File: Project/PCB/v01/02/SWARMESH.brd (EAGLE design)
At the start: 75 x 75 mm, 51 parts, among them T5 TIP122TIP122, U1 ESP32DEVKITC, U2 TCRT5000L, U3 L293D, U4 L7805CV, U5 TCRT5000L, U6 CD4051BEE4

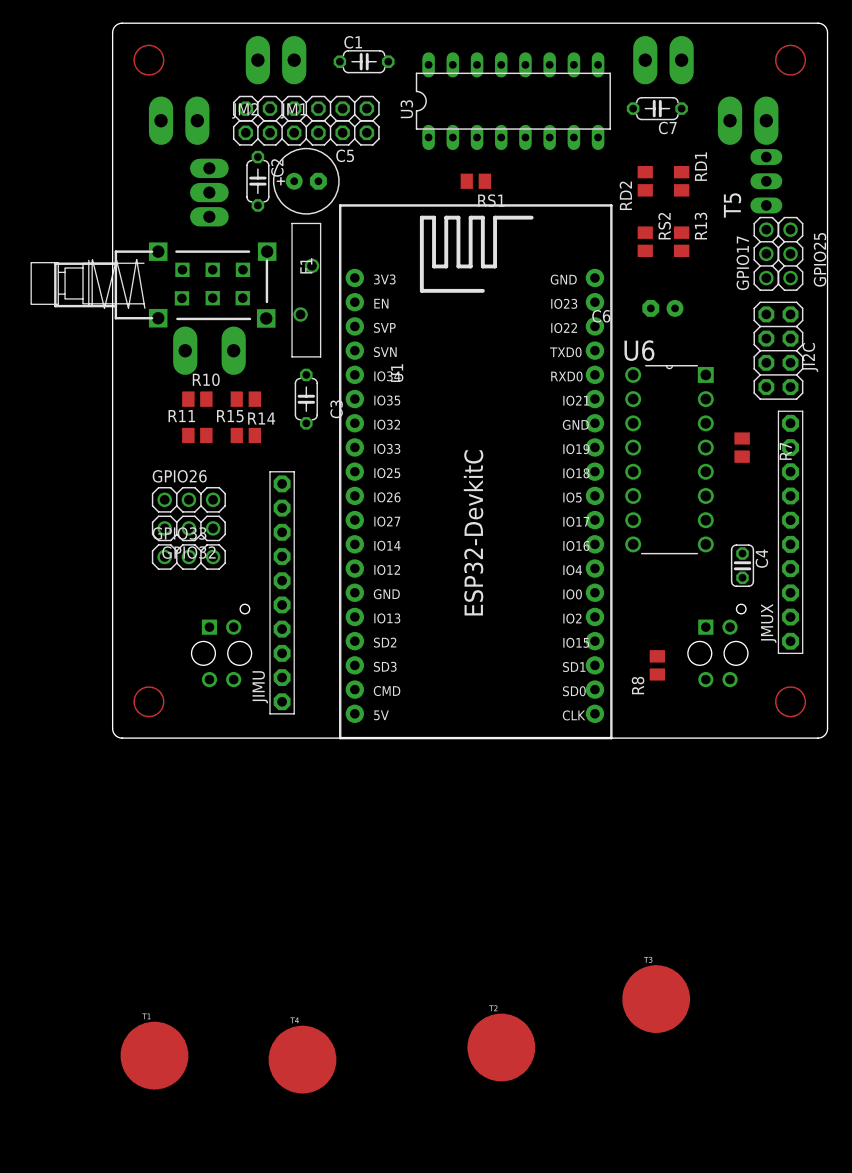
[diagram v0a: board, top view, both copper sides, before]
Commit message: add led PCB
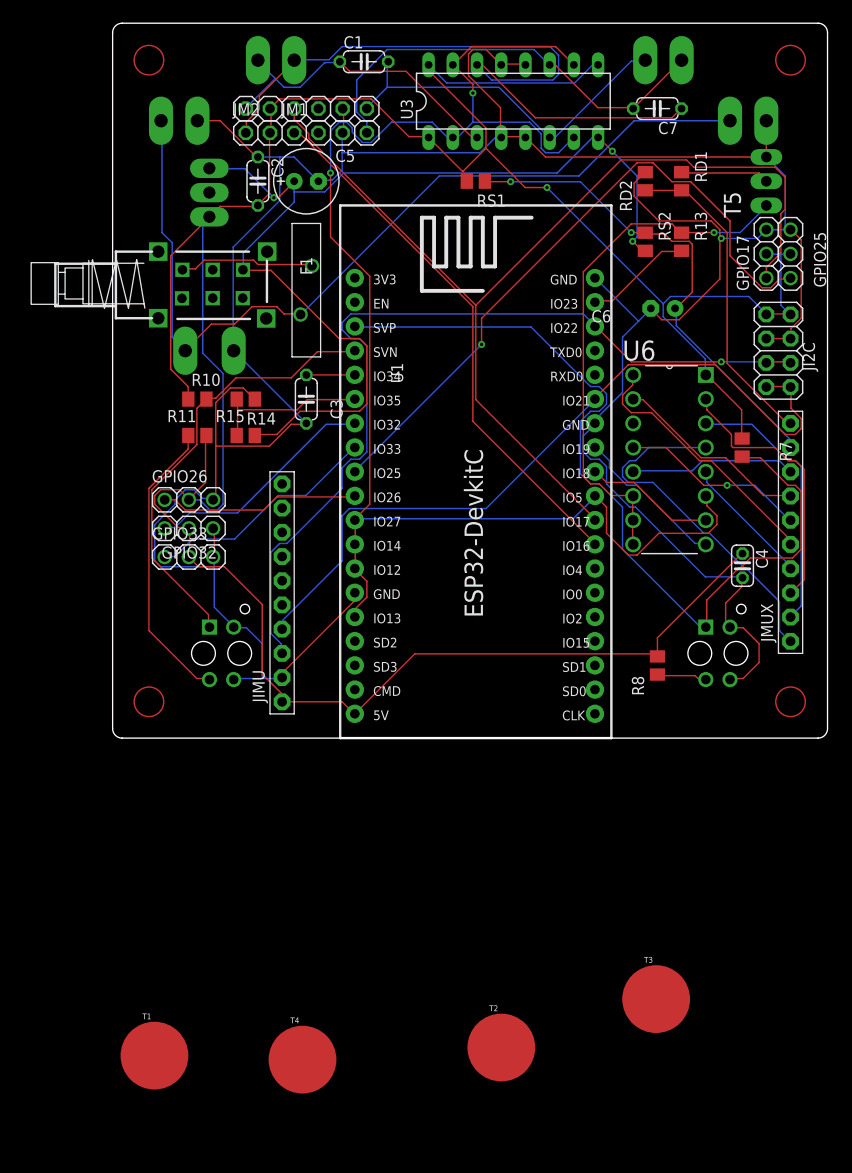
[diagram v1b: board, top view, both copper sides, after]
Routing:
- net GND: track 0.00 -> 328.8 mm, vias 0 -> 1
- net VCC: track 0.00 -> 298.0 mm, vias 0 -> 1
- net IO5: track 0.00 -> 155.9 mm, vias 0 -> 2
- net E1A: track 0.00 -> 107.2 mm
- net V+: track 0.00 -> 106.8 mm, vias 0 -> 3
- net N$15: track 0.00 -> 93.1 mm
- net SCL: track 0.00 -> 91.7 mm, vias 0 -> 1
- net IR1: track 0.00 -> 90.6 mm
- net SDA: track 0.00 -> 80.0 mm
- net M2A: track 0.00 -> 74.1 mm
- net IO25: track 0.00 -> 68.8 mm, vias 0 -> 1
- net E2A: track 0.00 -> 56.6 mm
- net N$12: track 0.00 -> 55.6 mm, vias 0 -> 1
- net N$16: track 0.00 -> 51.7 mm, vias 0 -> 2
- net IR2: track 0.00 -> 46.5 mm
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
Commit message: component placement
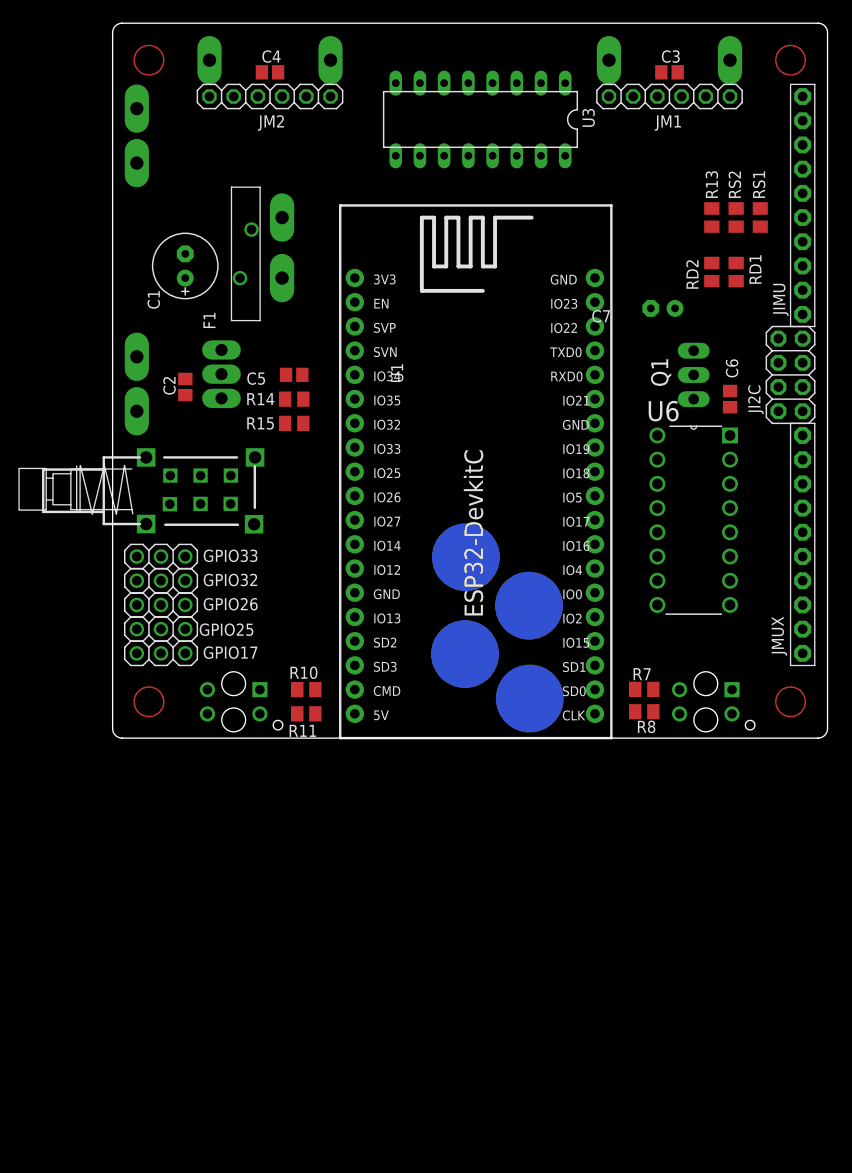
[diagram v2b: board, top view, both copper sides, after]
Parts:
- removed S2: (no value), ArduinoNano LearningBot 4-21-18:PS22F03
- removed T5: TIP122TIP122, TIP122(2):TIP122MODIFIED
- added Q1: TIP122TIP122, TIP122(2):TIP122MODIFIED
- added S1: (no value), ArduinoNano LearningBot 4-21-18:PS22F03
- C1, C7: value 0.1uF -> 10uF; device adafruit:C050-024X044 -> adafruit:E2,5-7
- C2, C3: value 0.1uF -> (none); device adafruit:C050-024X044 -> adafruit:C0805
- C4: value 0.1uF -> (none); device rcl:C025-024X044 -> adafruit:C0805
- C5, C6: value 10uF -> (none); device adafruit:E2,5-7 -> adafruit:C0805
- F1: value 30R400UF -> (none)
- moved GPIO25 76.9 mm to (5.08, 11.4), turned to 180 degrees
- moved GPIO17 76.1 mm to (5.08, 8.89), turned to 180 degrees
- moved C4 71.7 mm to (16.5, 69.8), turned to 0 degrees
- moved JIMU 68.1 mm to (72.4, 55.9)
- moved T4 55.4 mm to (37.1, 19.0), flipped to the bottom
- moved T1 54.3 mm to (43.8, 4.16), flipped to the bottom
- moved BAT- 53.4 mm to (17.8, 48.3)
- moved C3 51.3 mm to (58.4, 69.8), turned to 0 degrees
- moved CHG2+ 48.1 mm to (17.8, 54.6)
- moved T3 43.4 mm to (43.7, 13.9), flipped to the bottom
- moved T2 41.5 mm to (37.0, 8.81), flipped to the bottom
- moved JM1 38.1 mm to (58.4, 67.3)
- moved JP1 36.8 mm to (52.1, 71.1)
- moved JP3 36.8 mm to (22.9, 71.1)
- moved R10 32.6 mm to (20.3, 5.08), turned to 180 degrees
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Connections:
- removed net ADCMX1: U6.3
- new net IO12: U1.13, U3.15
- new net IO13: U1.15, U3.10
- new net IO14: U1.12, U3.2
- new net IO27: U1.11, U3.7
- net ADCMX: now also C5.1, U6.3; no longer C3.1
- net GND: now also C1.-, C5.2, C6.2, C7.-, Q1.3, U4.2; no longer C3.2, C4.2, C5.-, C6.-, T5.3
- net IO5: no longer U1.11, U1.12, U1.13, U1.15, U3.10, U3.15, U3.2, U3.7
- net M1A: now also C3.1; no longer C1.1
- net M1B: now also C3.2; no longer C1.2
- net M2A: now also C4.1; no longer C7.1
- net M2B: now also C4.2; no longer C7.2
- net N$1: now also Q1.2; no longer T5.2
- net N$12: now also Q1.1; no longer T5.1
- net N$16: now also C7.+; no longer C6.+
- net N$18: now also S1.NC1; no longer S2.NC1
- net V+: now also C1.+, S1.NO1; no longer C5.+, S2.NO1
- net VCC: now also C6.1; no longer C4.1
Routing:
- net GND: track 328.8 -> 0.00 mm, vias 1 -> 0
- net VCC: track 298.0 -> 0.00 mm, vias 1 -> 0
- net IO5: track 155.9 -> 0.00 mm, vias 2 -> 0
- net E1A: track 107.2 -> 0.00 mm
- net V+: track 106.8 -> 0.00 mm, vias 3 -> 0
- net N$15: track 93.1 -> 0.00 mm
- net SCL: track 91.7 -> 0.00 mm, vias 1 -> 0
- net IR1: track 90.6 -> 0.00 mm
- net SDA: track 80.0 -> 0.00 mm
- net M2A: track 74.1 -> 0.00 mm
- net IO25: track 68.8 -> 0.00 mm, vias 1 -> 0
- net E2A: track 56.6 -> 0.00 mm
- net N$12: track 55.6 -> 0.00 mm, vias 1 -> 0
- net N$16: track 51.7 -> 0.00 mm, vias 2 -> 0
- net IR2: track 46.5 -> 0.00 mm
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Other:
- board text added: "Licensing: Creative Commons ShareAlike 4.0 International - https://creativecommons.org/licenses/by-sa/4.0/ You are welcome to use this library for commercial purposes. For attribution, we ask that when you reproduce our board, you email us with a link. Acknowlewdgement: This project has been supported by NYU Shanghai Dean's Undergraduate Research Fund."
- board text added: "NYU Shanghai Swarm Robotics Zander Mao Sheldon Chen Alison Yao Thomas Yee James Wu Benny Yang Rodolfo Cossovich 2019/06/25"
- board text added: "Notes: tip122 and 7805 have no component body. designators have different font size and are not aligned. Switch designator missing. It seems that many footprints overlap silkscreen to solder pads. Pin 1 should be indicated in any connector. Touch pads are too big and could have a hole to solder a cable. Positive and negative pads for battery look the same (they should have slikscreen marks and di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"

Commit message: tested with autorouting
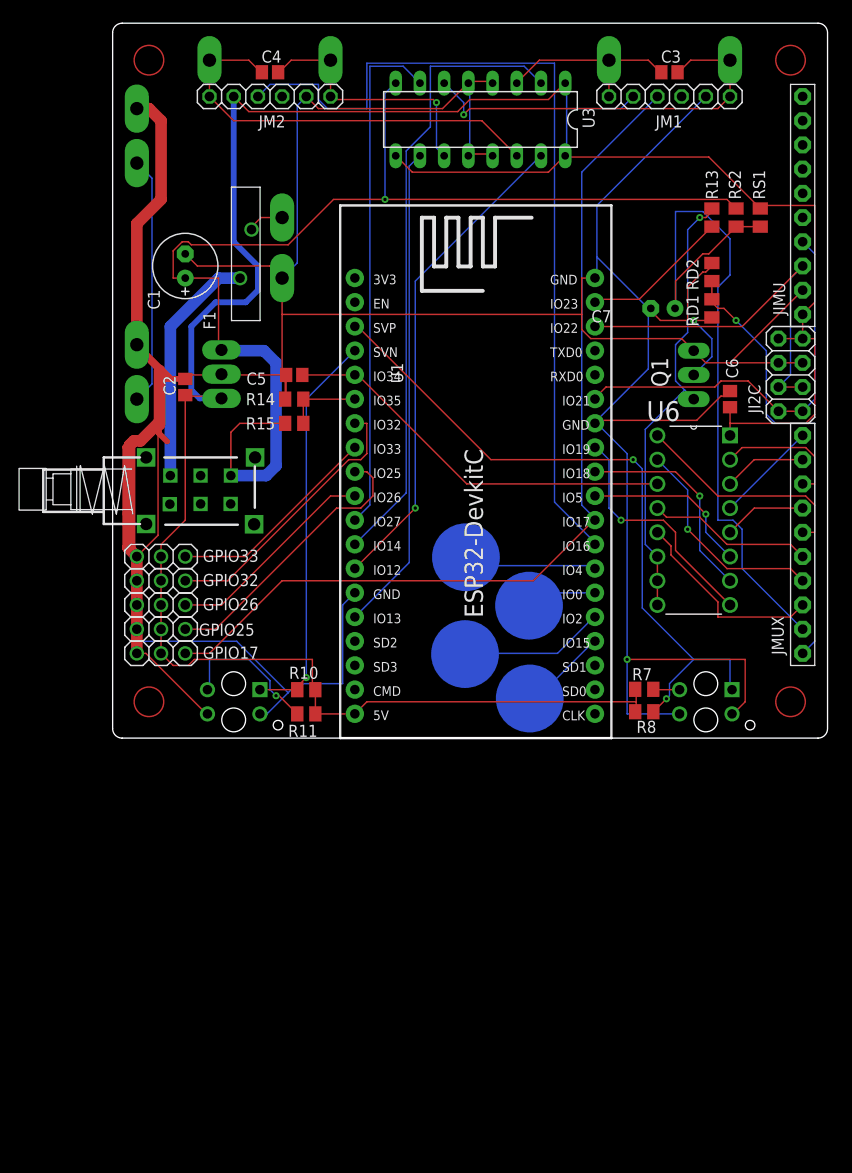
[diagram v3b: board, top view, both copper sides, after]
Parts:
- moved RD1 4.58 mm to (62.9, 45.1), turned to 90 degrees
- moved CHG1+ 1.27 mm to (2.54, 35.6)
- moved CHG1- 1.27 mm to (2.54, 41.3)
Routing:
- net GND: track 0.00 -> 473.9 mm, vias 0 -> 1
- net VCC: track 0.00 -> 270.3 mm
- net V+: track 0.00 -> 122.8 mm, vias 0 -> 1
- net E1A: track 0.00 -> 97.0 mm
- net E2A: track 0.00 -> 90.6 mm
- net N$16: track 0.00 -> 77.4 mm
- net IR1: track 0.00 -> 73.0 mm, vias 0 -> 2
- net IO14: track 0.00 -> 65.8 mm
- net IO27: track 0.00 -> 54.3 mm
- net IO12: track 0.00 -> 51.4 mm, vias 0 -> 1
- net IO13: track 0.00 -> 51.2 mm
- net N$12: track 0.00 -> 47.5 mm, vias 0 -> 1
- net N$17: track 0.00 -> 46.8 mm, vias 0 -> 1
- net M2A: track 0.00 -> 44.7 mm
- net SDA: track 0.00 -> 42.8 mm
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
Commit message: update win file
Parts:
- removed C7: 10uF, adafruit:E2,5-7
- removed RS2: 150, adafruit:M0805
- removed U4: L7805CV, L7805:L7805CV_FOOTPRINT
- added IC1: L7805CV-DG, L7805CV-DG:TO270P460X1020X2008-3P
- C1: device adafruit:E2,5-7 -> adafruit:E2-5
- C3, C4, C6: device adafruit:C0805 -> adafruit:C025-025X050
- C5: device adafruit:C0805 -> adafruit:C025-030X050
- F1: value (none) -> RUEF300K-2; device 30R400UF:30R400UF -> RUEF300K-2:RUEF300K2
- Q1: value TIP122TIP122 -> TIP122; device TIP122(2):TIP122MODIFIED -> TIP122:TO270P460X1020X2008-3P
- R10, R11, R13, R14, R15, R7, R8, RD1, RD2: device adafruit:M0805 -> adafruit:0207/9
- RS1: value 150 -> 220; device adafruit:M0805 -> adafruit:0207/9
- moved T2 50.4 mm to (24.9, -40.1)
- moved T3 48.3 mm to (15.7, -25.5)
- moved T4 38.9 mm to (15.5, -13.4)
- moved T1 32.4 mm to (43.8, -28.2)
- moved U2 27.6 mm to (39.4, 10.8), turned to 270 degrees
- moved U5 16.2 mm to (65.4, -12.1)
- moved F1 13.6 mm to (7.62, 62.9)
- moved RS1 11.4 mm to (61.6, 64.1), turned to 180 degrees
- moved RD1 8.28 mm to (63.5, 53.3), turned to 0 degrees
- moved CHG2- 7.62 mm to (2.54, 58.4)
- moved R8 7.24 mm to (60.2, 10.8)
- moved R10 6.02 mm to (18.4, 10.8), turned to 0 degrees
- moved R7 5.46 mm to (60.2, 5.95)
- moved R13 5.43 mm to (61.0, 59.7), turned to 0 degrees
- moved BAT+ 3.81 mm to (2.54, 64.1)
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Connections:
- net GND: now also IC1.2; no longer C7.-, U4.2
- net N$16: no longer C7.+, RS2.1
- net V+: now also IC1.1; no longer RS2.2, U4.1
- net VCC: now also IC1.3; no longer U4.3
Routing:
- net V+: track 122.8 -> 82.8 mm
- net IR1: track 73.0 -> 98.6 mm
- net N$10: track 2.77 -> 23.6 mm
- net N$15: track 30.4 -> 49.4 mm
- net N$9: track 15.5 -> 31.5 mm
- net N$16: track 77.4 -> 62.1 mm, vias 0 -> 1
- net TOUCH2: track 15.2 -> 0.12 mm
- net TOUCH4: track 14.6 -> 0.00 mm
- net VCC: track 270.3 -> 280.5 mm
- net TOUCH1: track 9.45 -> 0.00 mm
- net IR2: track 42.1 -> 51.4 mm
- net IRTX: track 15.6 -> 24.2 mm
- net N$1: track 9.52 -> 17.6 mm
- net TOUCH3: track 8.21 -> 0.12 mm
- net N$18: track 25.1 -> 31.1 mm
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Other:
- board text added: "This IR reflective sensor should be standing in the front of the robot so we use it to detect obstacles."
- board text added: "Zander's update: Changed TIP122&L7805CV footprint Changed resister to PTH Romain's Suggestions: leave the ground pin first, use ground plane to connect them later"
